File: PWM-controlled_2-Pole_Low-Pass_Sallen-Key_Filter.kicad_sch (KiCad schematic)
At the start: 20 parts, among them J1 Audio_In, J2 PWM1, J3 PWM2, J4 3.3V_IN, J5 Unused_OpAmp, J6 Audio_Output, U1 NSL-32, U2 NSL-32, U3 TLV2372

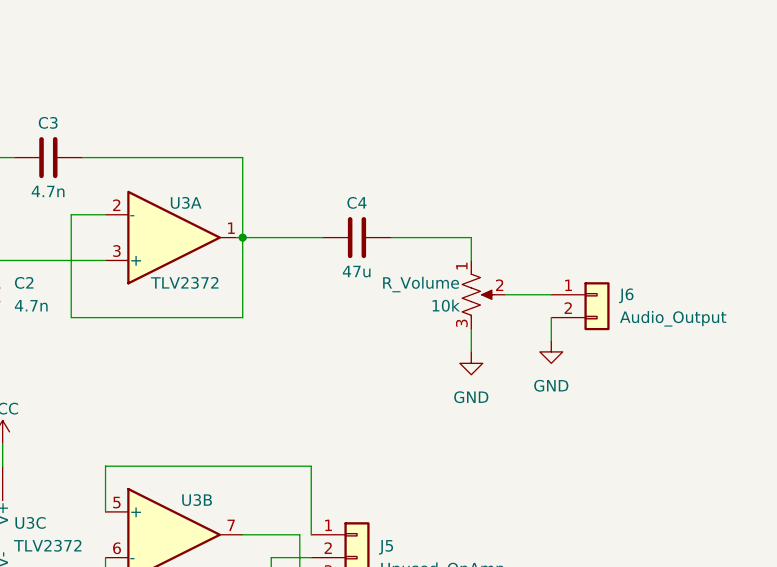
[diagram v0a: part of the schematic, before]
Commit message: Update PWM-controlled_2-Pole_Low-Pass_Sallen-Key_Filter.kicad_sch
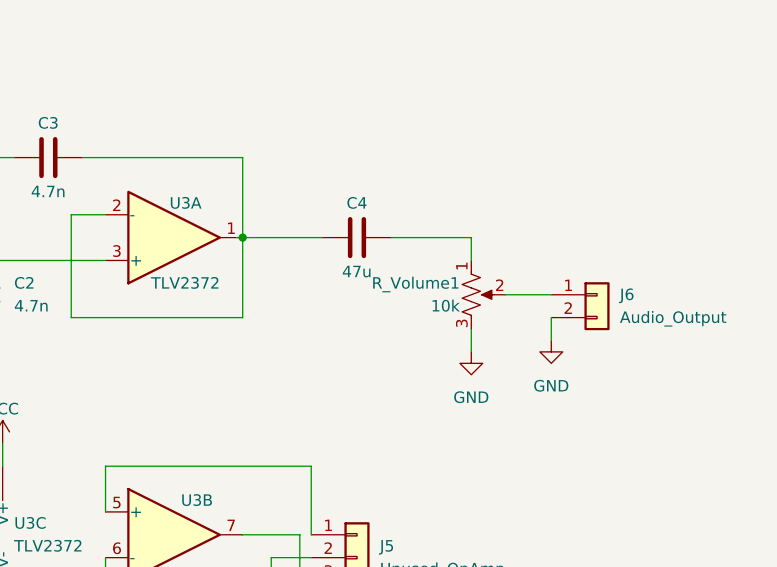
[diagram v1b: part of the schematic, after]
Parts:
- renumbered R_Volume to R_Volume1
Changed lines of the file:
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@@
 		(on_board yes)
 		(dnp no)
-		(property "Reference" "R_Volume"
+		(property "Reference" "R_Volume1"
 			(at 154.94 87.63 0)
 			(effects
@@
 			(project ""
 				(path "/fa0e25e8-ac7a-409d-b2e9-0acfbfd2e50e"
-					(reference "R_Volume")
+					(reference "R_Volume1")
 					(unit 1)
 				)
